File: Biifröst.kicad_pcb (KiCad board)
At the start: 2 copper layers, 42 x 84 mm, 18 parts, among them J1 Pitaya_Go, J2 LCD_SPI, J3 SPI_SD, J4 CMSIS-DAP, J5 DEBUG UART *DNP*, SW1 JS1400AFQ, SW2 TL9100AF200Q, SW3 TL9100AF200Q

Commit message: Update pins to have not bars where they should be.
And fixed a dumb typo on a net name.
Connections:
- net /ALT_CS renamed /~ALT_CS~
- net /INPUIT_LEFT renamed /INPUT_LEFT
- net /LCD_CS renamed /~LCD_CS~
- net /LCD_DC renamed /LCD_D~C~
- net /LCD_RST renamed /~LCD_RST~
- net /SD_CS renamed /~SD_CS~
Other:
- board text added: "D~C~"
- board text added: "~CS~"
- board text added: "~RESET~"
- board text added: "~RST~/P0.18"
- board text removed: "CS"
- board text removed: "DC"
- board text removed: "RST"
- board text removed: "RST/P0.18"

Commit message: Add/adjust some silks. Bump to r1.
Still need to test the apa102 at 3.3v before I send it up for another spin.
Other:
- board text added: "RX"
- board text added: "Revision 1"
- board text added: "TX"
- board text added: "~ALT_CS~"
- board text added: "~RST~"
- board text removed: "ALT_CS"
- board text removed: "Revision 0"

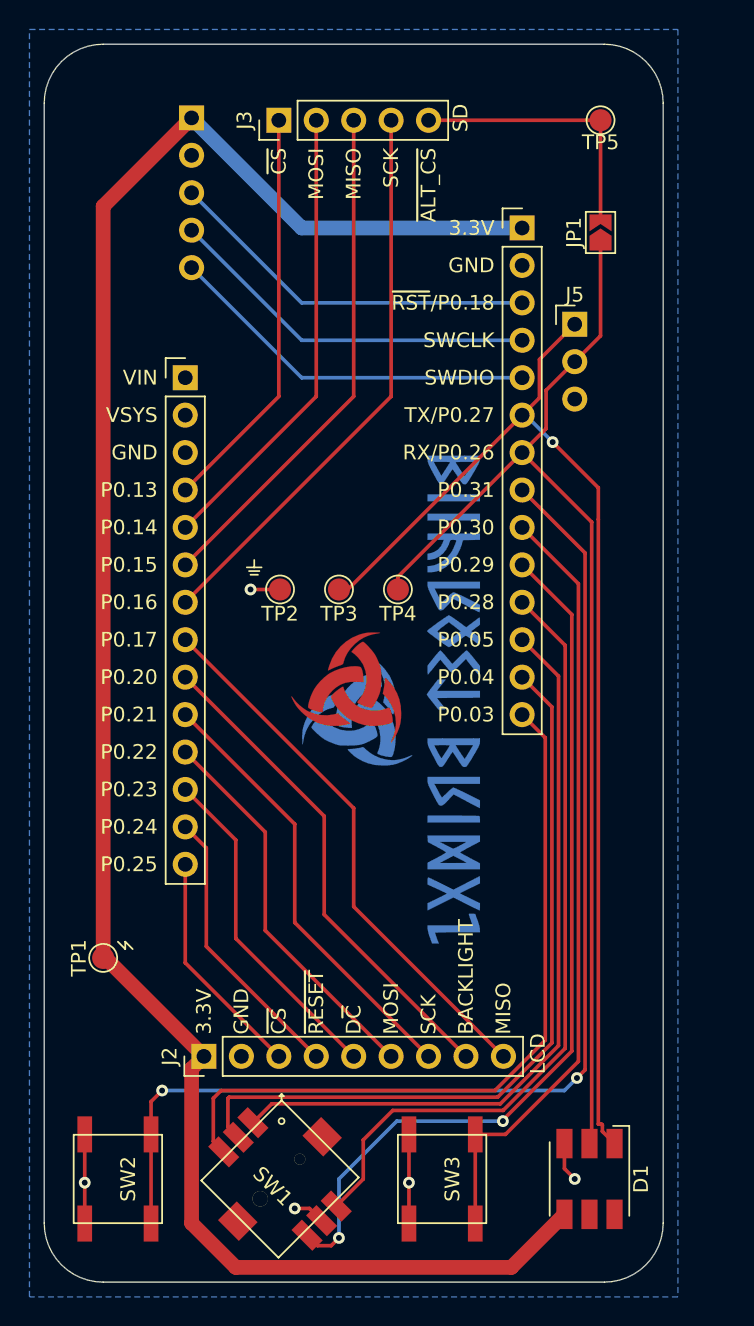
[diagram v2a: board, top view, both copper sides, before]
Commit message: Add VIN/VSYS breakout. Add 4 hole cuts that will line up with sister boards.
2 hole cuts will align with the pitaya go holes (1 top, 1 bottom, on one side)
2 hole cuts will align with the LCD board holes (1 top, 1 bottom, opposite side from pitaya.)

Not perfectly ideal, but required no trace moves, and they may be useful.
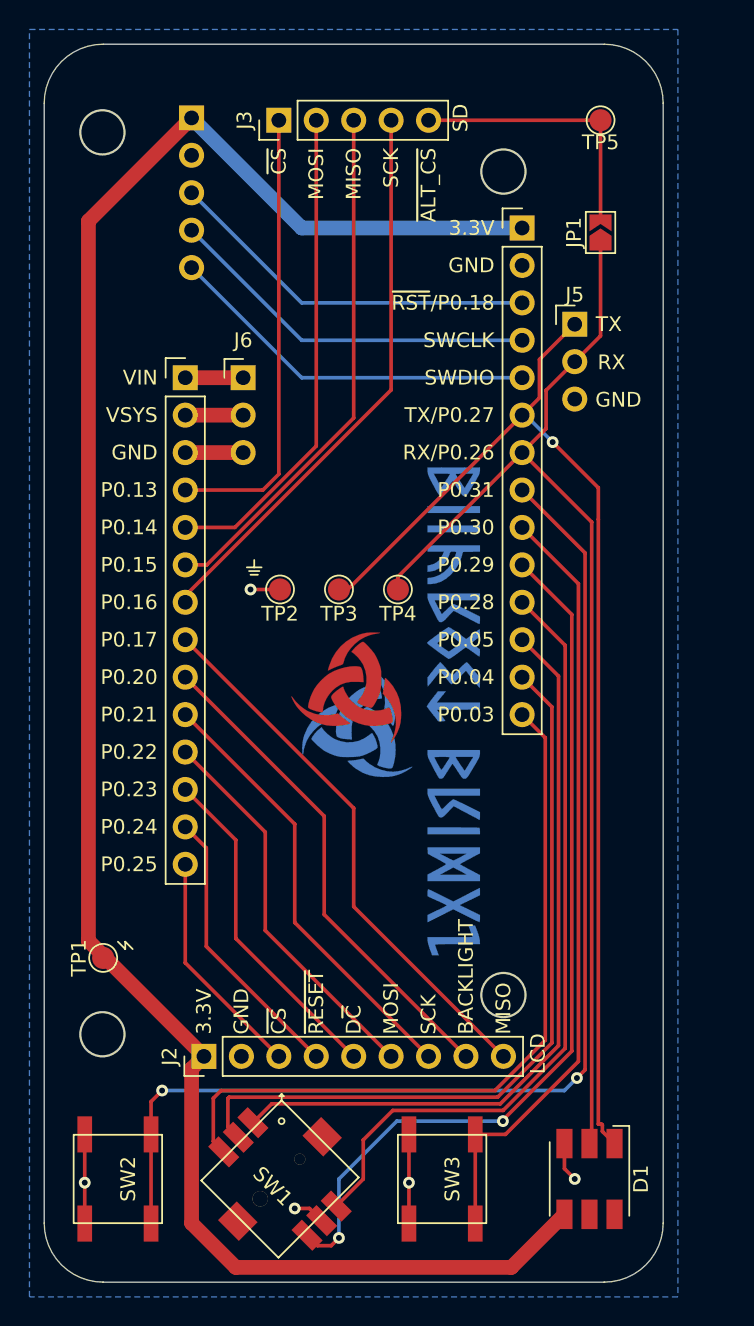
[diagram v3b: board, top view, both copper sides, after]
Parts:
- added J6: OPT PWR *DNP*, Connector_PinHeader_2.54mm:PinHeader_1x03_P2.54mm_Horizontal, F.Cu at (13.5, 22.6)
- moved Ref** 0.80 mm to (28.0, 45.2)
- moved Ref** 0.78 mm to (21.6, 46.5)
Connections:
- J1 pad 1: Net-(J1-Pad1) -> /VIN
- J1 pad 2: Net-(J1-Pad2) -> /VSYS
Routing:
- net GND: track 19.0 -> 22.9 mm
- net /VSYS: track 0.00 -> 3.93 mm
- net /VIN: track 0.00 -> 3.93 mm
- net /~SD_CS~: track 27.7 -> 30.8 mm
- net /SD_MOSI: track 31.3 -> 33.3 mm
- net /SD_MISO: track 34.9 -> 35.8 mm
- net +3V3: track 134.2 -> 135.1 mm
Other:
- outline, holes or cut-outs redrawn
- board text added: "VIN (4.5-6.4V)"
- board text added: "VSYS 4.4V/2A OUT"
